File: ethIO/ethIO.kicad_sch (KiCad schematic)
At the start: 0 parts

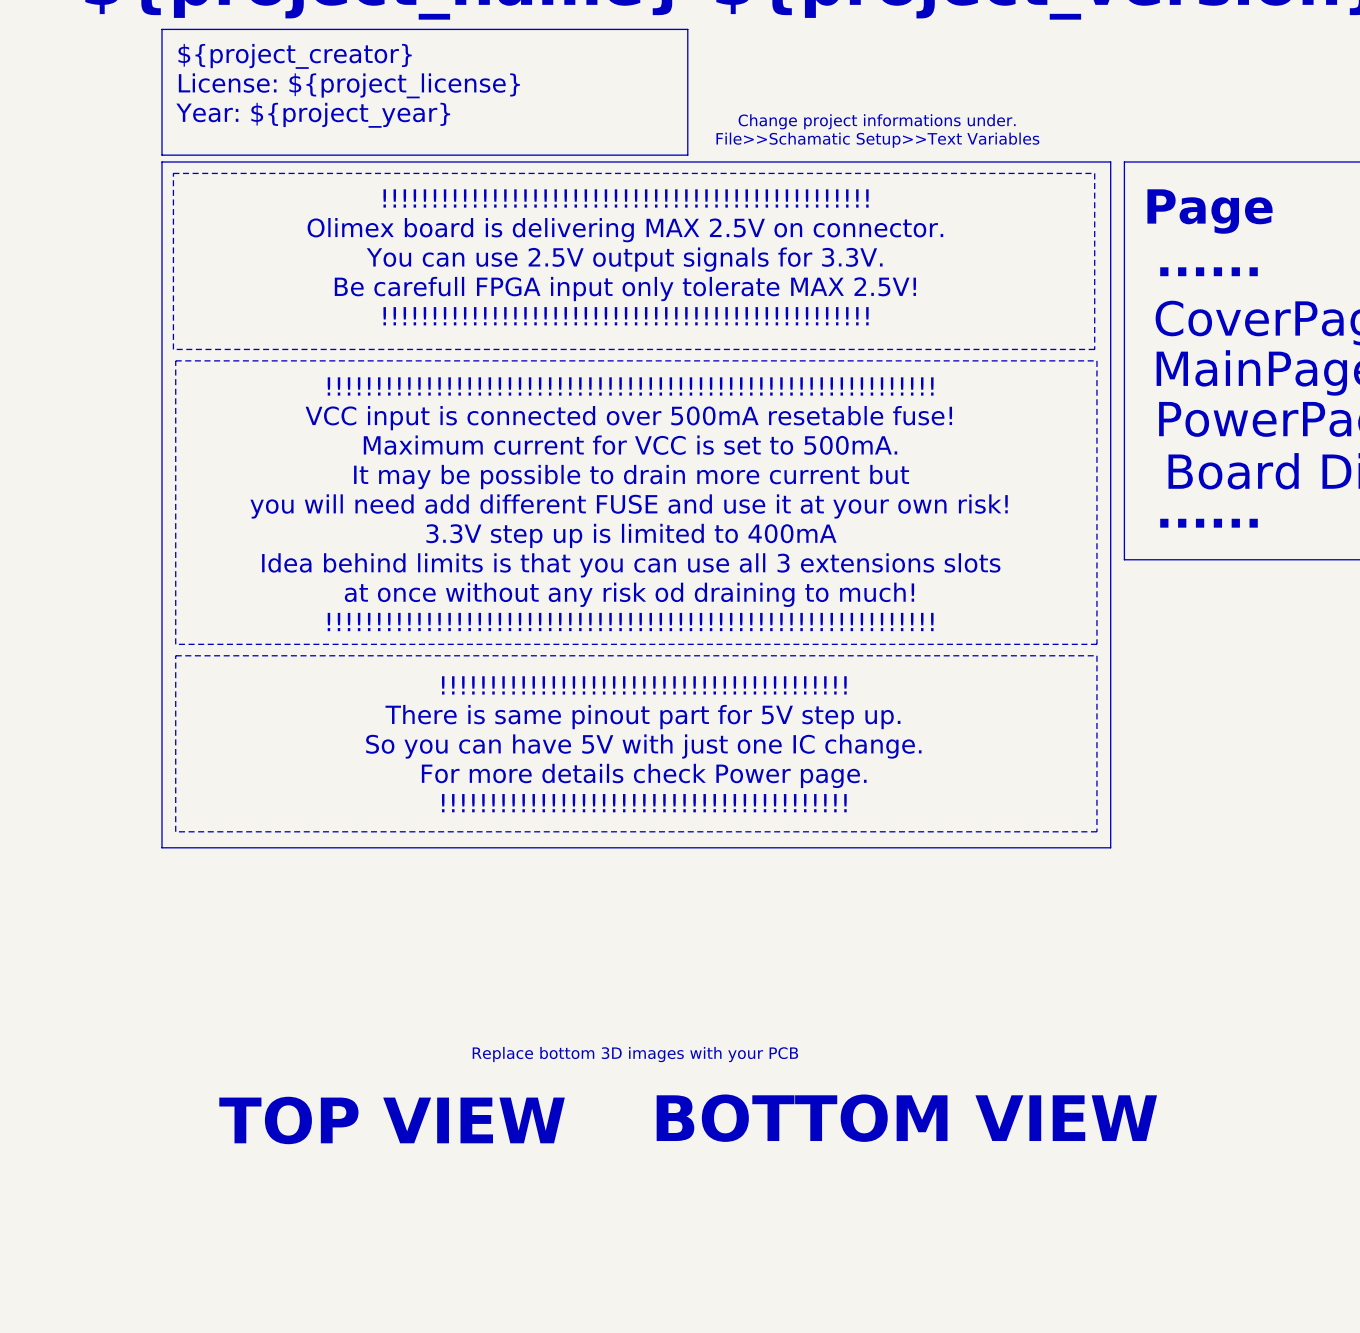
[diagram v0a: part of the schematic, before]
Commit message: Updating ethIO
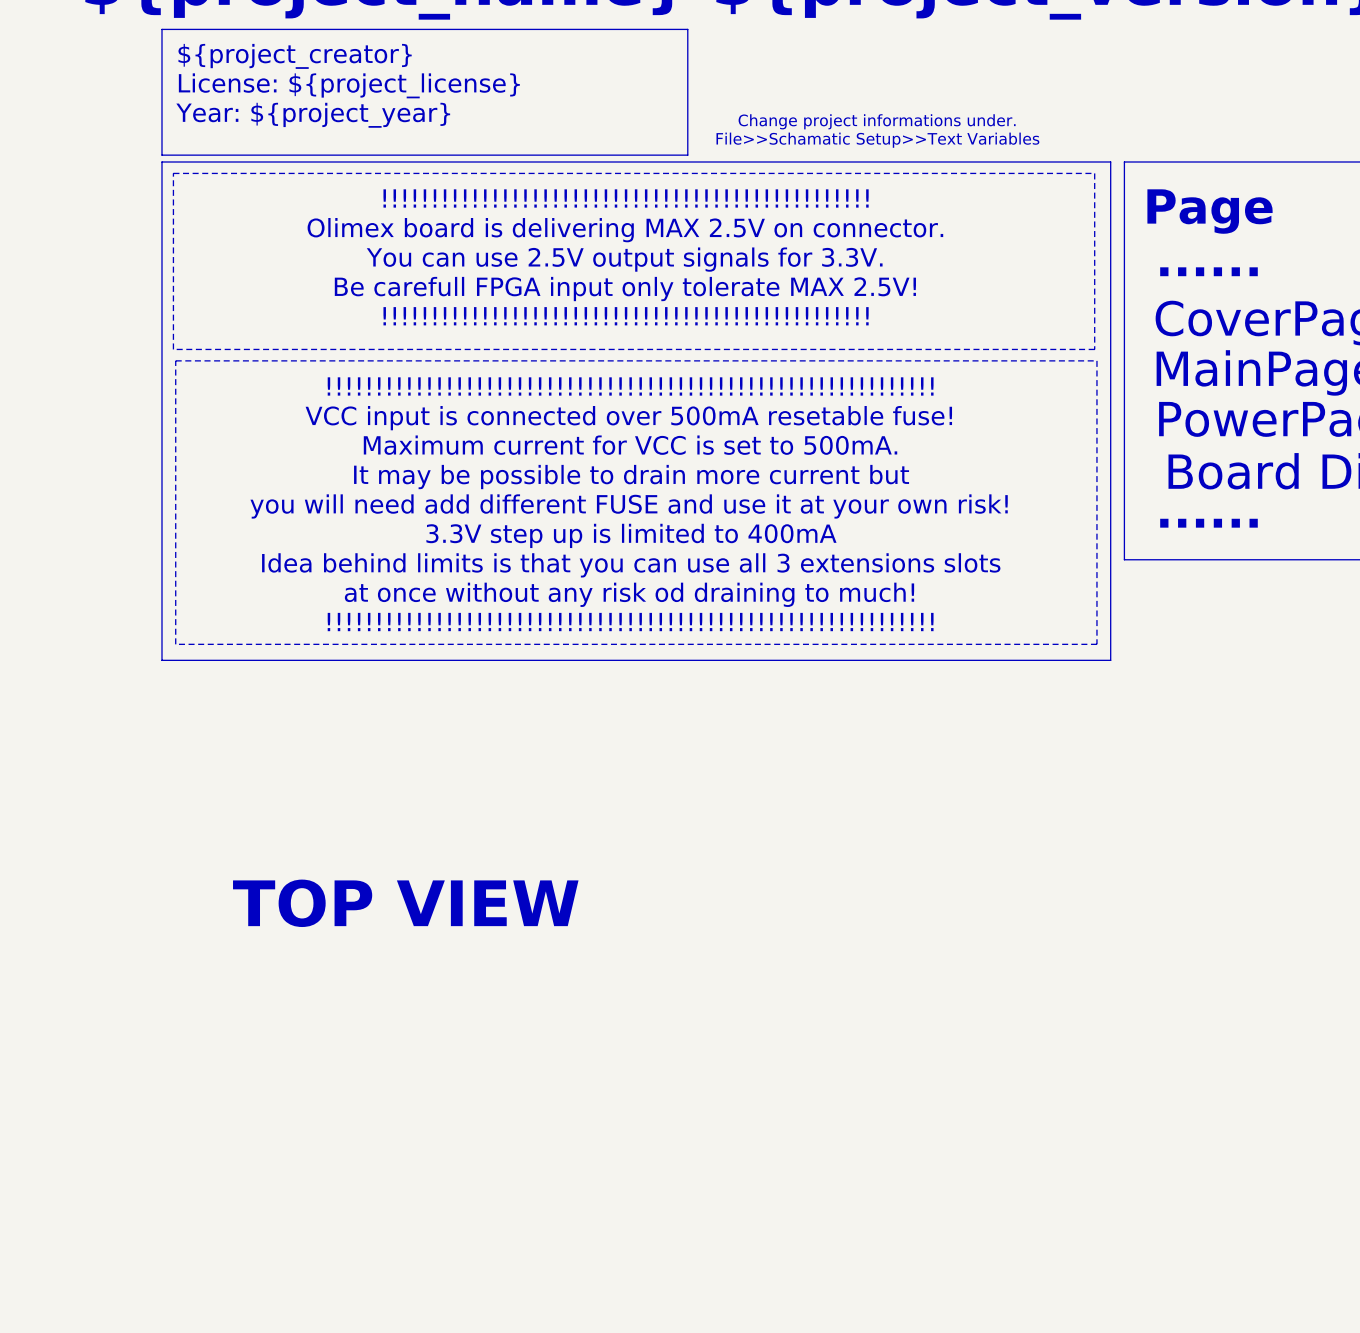
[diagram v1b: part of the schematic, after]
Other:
- note removed: "!!!!!!!!!!!!!!!!!!!!!!!!!!!!!!!!!!!!!!!!! There is same pinout part for 5V step up. So you can have 5V with just one IC change. For more details check Power page. !!!!!!!!!!!!!!!!!!!!!!!!!!!!!!!!!!!!!!!!!"
- note removed: "BOTTOM VIEW"
- note removed: "Replace bottom 3D images with your PCB"
